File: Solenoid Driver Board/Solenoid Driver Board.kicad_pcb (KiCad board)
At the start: 2 copper layers, 33.5 x 39.6 mm, 22 parts, among them J2 Solenoid, Q1 IRLB8721PBF, U1 AMS1117-5.0, U2 STM8S003F3P, Y1 Crystal

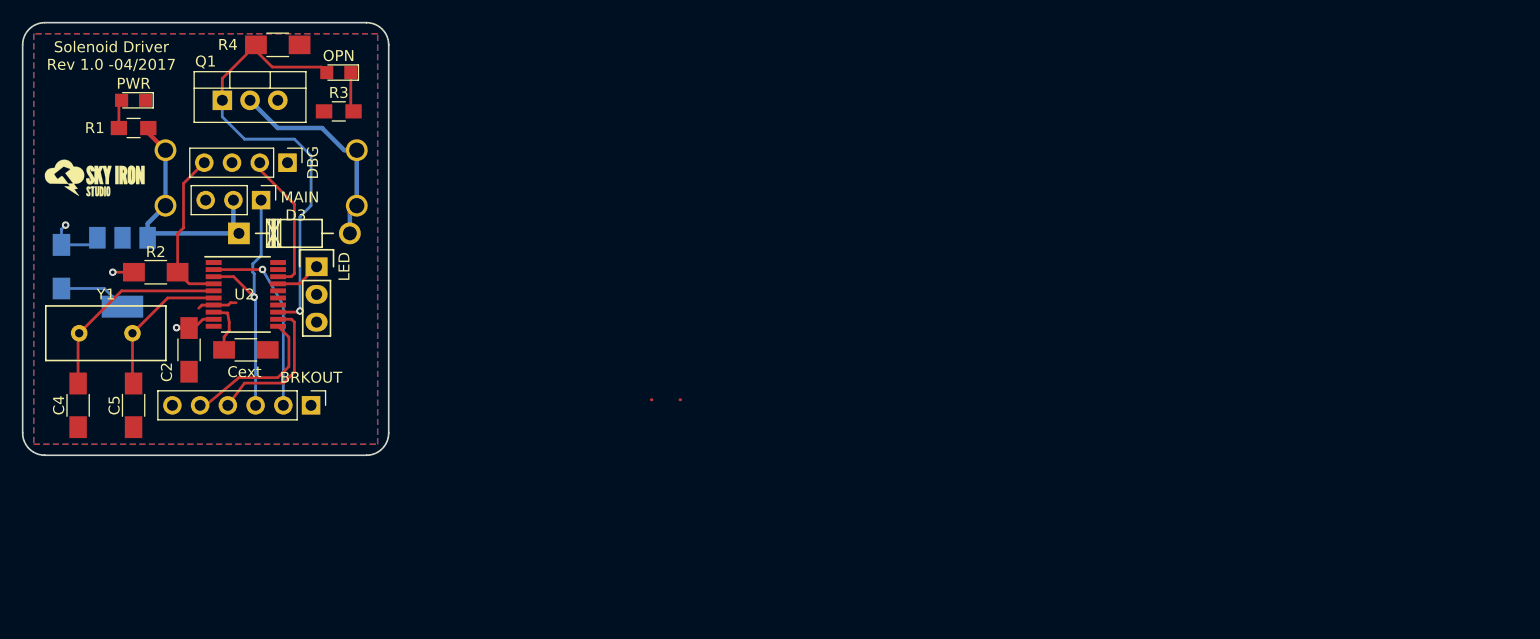
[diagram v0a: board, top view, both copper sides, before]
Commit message: Moved fade to TIM4, started work on new board revision
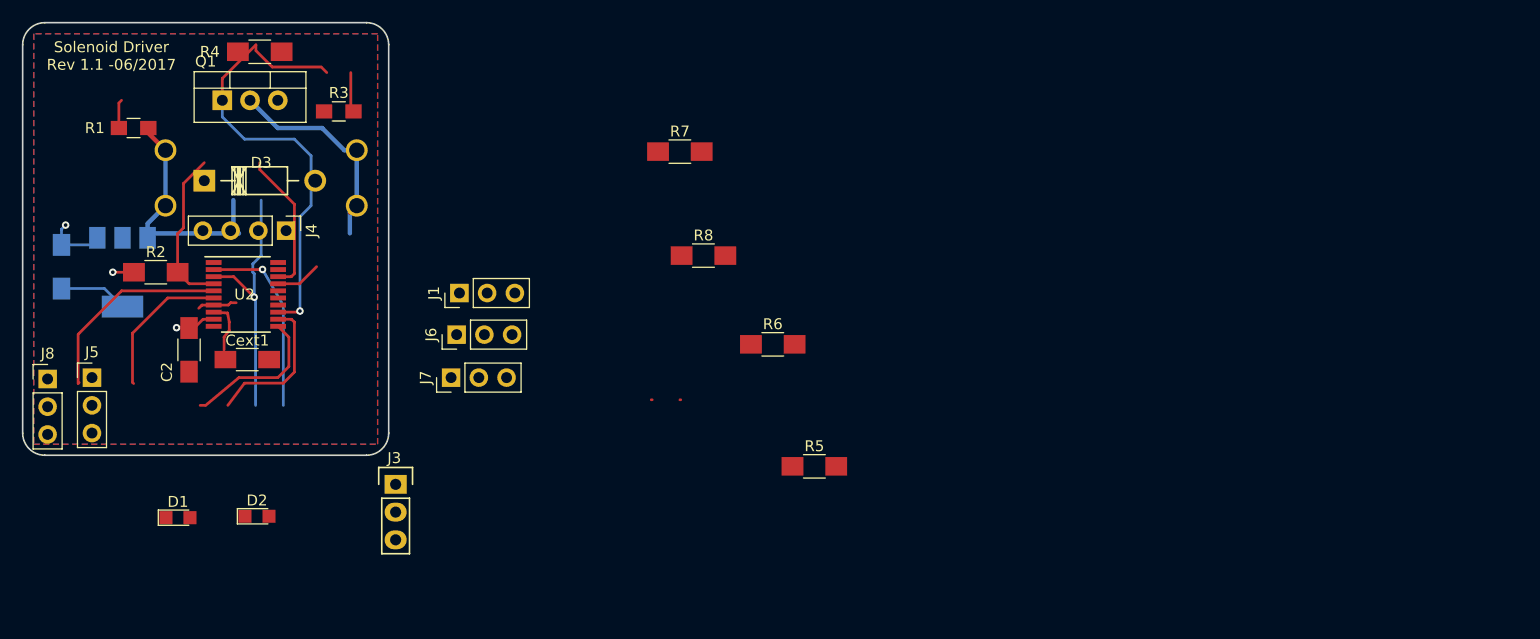
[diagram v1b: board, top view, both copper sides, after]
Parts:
- removed BRKOUT: BREAKOUT, Pin_Headers:Pin_Header_Straight_1x06_Pitch2.54mm
- removed C4, C5: 22pf, Capacitors_SMD:C_1206_HandSoldering
- removed Cext: 1 uF, Capacitors_SMD:C_1206_HandSoldering
- removed DBG: DEBUG, Pin_Headers:Pin_Header_Straight_1x04_Pitch2.54mm
- removed G***: LOGO, Modules:SkyIronLogo
- removed LED: RGB_LED, Pin_Headers:Pin_Header_Straight_1x03
- removed MAIN: MAIN, Pin_Headers:Pin_Header_Straight_1x03_Pitch2.54mm
- removed OPN: ON, LEDs:LED_0805
- removed PWR: PWR, LEDs:LED_0805
- removed Y1: Crystal, SpadeConnector:Crystal_HC-49-S
- added Cext1: 1 uF, Capacitors_SMD:C_1206_HandSoldering, F.Cu at (119.1, 103.0)
- added D1: PWR, LEDs:LED_0805, F.Cu at (112.8, 117.5)
- added D2: ON, LEDs:LED_0805, F.Cu at (120.0, 117.3)
- added J1: CH1, Pin_Headers:Pin_Header_Straight_1x03_Pitch2.54mm, F.Cu at (138.6, 96.9)
- added J3: RGB_LED, Pin_Headers:Pin_Header_Straight_1x03, F.Cu at (132.7, 114.4)
- added J4: DEBUG, Pin_Headers:Pin_Header_Straight_1x04_Pitch2.54mm, F.Cu at (122.7, 91.2)
- added J5: MAIN, Pin_Headers:Pin_Header_Straight_1x03_Pitch2.54mm, F.Cu at (104.9, 104.6)
- added J6: CH2, Pin_Headers:Pin_Header_Straight_1x03_Pitch2.54mm, F.Cu at (138.3, 100.7)
- added J7: CH3, Pin_Headers:Pin_Header_Straight_1x03_Pitch2.54mm, F.Cu at (137.8, 104.6)
- added J8: MAIN, Pin_Headers:Pin_Header_Straight_1x03_Pitch2.54mm, F.Cu at (100.8, 104.8)
- added R5: 10k, Resistors_SMD:R_1206_HandSoldering, F.Cu at (171.1, 112.8)
- added R6: 10k, Resistors_SMD:R_1206_HandSoldering, F.Cu at (167.3, 101.6)
- added R7: 10k, Resistors_SMD:R_1206_HandSoldering, F.Cu at (158.8, 83.9)
- added R8: 10k, Resistors_SMD:R_1206_HandSoldering, F.Cu at (160.9, 93.5)
- moved D3 5.78 mm to (115.2, 86.6)
- moved R4 1.77 mm to (120.3, 74.8)
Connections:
- U2 pad 10: (no net) -> CH3
- U2 pad 11: PB5 -> (no net)
- U2 pad 12: PB4 -> (no net)
- U2 pad 15: (no net) -> CH1
- U2 pad 19: (no net) -> VIN_A
- U2 pad 2: TX -> (no net)
- U2 pad 20: (no net) -> CH2
- U2 pad 5: Net-(C4-Pad2) -> (no net)
- U2 pad 6: Net-(C5-Pad2) -> (no net)
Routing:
- net (no net): track 0.16 -> 77.0 mm, vias 0 -> 1
- net Net-(C4-Pad2): track 18.7 -> 0.00 mm
- net TX: track 17.4 -> 0.00 mm, vias 1 -> 0
- net PB4: track 13.7 -> 0.00 mm
- net PB5: track 13.6 -> 0.00 mm
- net Net-(C5-Pad2): track 13.4 -> 0.00 mm
- net GND: track 9.16 -> 12.4 mm
- net +12V: track 23.6 -> 20.4 mm
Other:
- board text added: "Solenoid Driver Rev 1.1 -06/2017"
- board text removed: "0V"
- board text removed: "12V"
- board text removed: "5V"
- board text removed: "DAT"
- board text removed: "GND"
- board text removed: "PB4"
- board text removed: "PB5"
- board text removed: "RX"
- board text removed: "SCL"
- board text removed: "SDA"
- board text removed: "SW"
- board text removed: "Solenoid Driver Rev 1.0 -04/2017"
- board text removed: "TX"
- board text removed: "~RST"

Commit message: Layout work begun on v1.1 of PCB
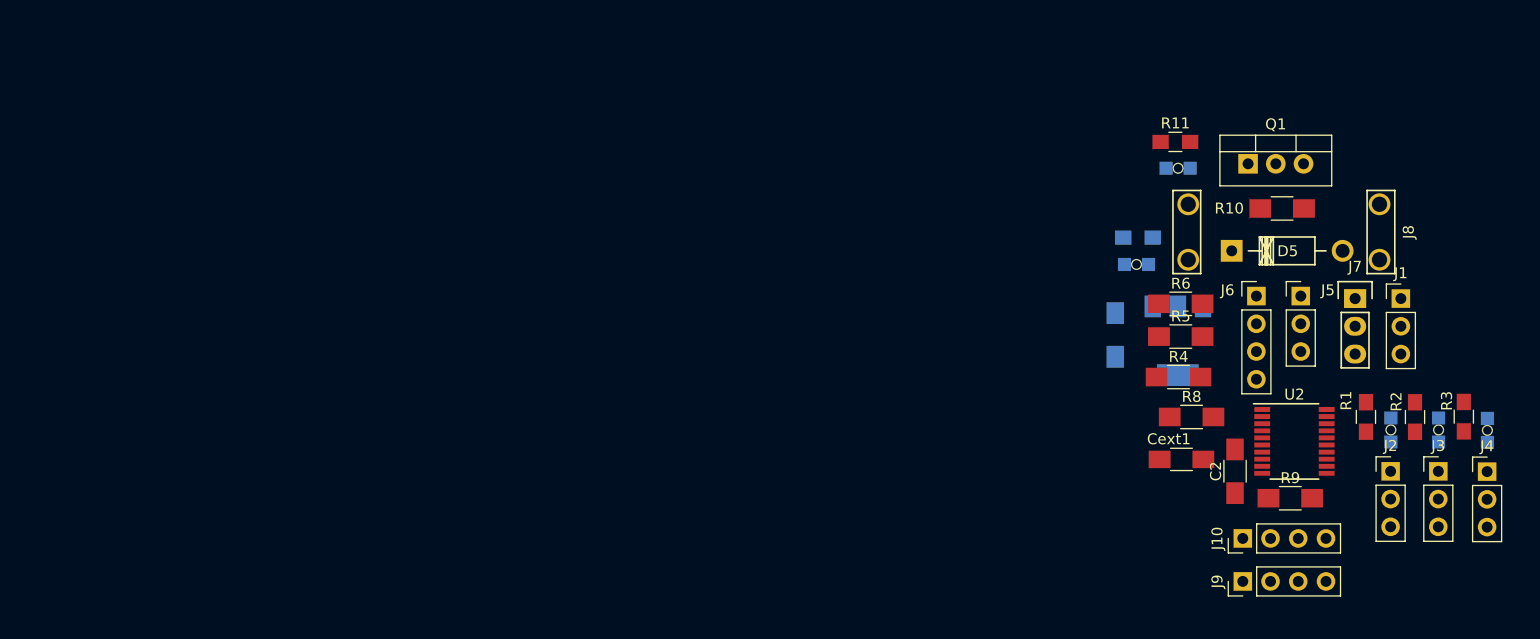
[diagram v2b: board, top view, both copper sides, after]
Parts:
- added D4: PWR, SpadeConnector:LED_0805_Bottom_Hole, B.Cu at (200.6, 94.3)
- added D5: 1N4007, Diodes_THT:Diode_DO-41_SOD81_Horizontal_RM10, F.Cu at (209.3, 93.0)
- added D6: ON, SpadeConnector:LED_0805_Bottom_Hole, B.Cu at (204.4, 85.5)
- added J10: DEBUG, Pin_Headers:Pin_Header_Straight_1x04_Pitch2.54mm, F.Cu at (210.3, 119.4)
- added J9: I2C, Pin_Headers:Pin_Header_Straight_1x04_Pitch2.54mm, F.Cu at (210.3, 123.3)
- added R10: 10K, Resistors_SMD:R_1206_HandSoldering, F.Cu at (213.9, 89.2)
- added R11: 330, Resistors_SMD:R_0805_HandSoldering, F.Cu at (204.1, 83.1)
- added R9: 10k, Resistors_SMD:R_1206_HandSoldering, F.Cu at (214.7, 115.7)
- D1: value PWR -> ON; footprint LEDs:LED_0805 -> SpadeConnector:LED_0805_Bottom_Hole; moved to B.Cu
- D2: footprint LEDs:LED_0805 -> SpadeConnector:LED_0805_Bottom_Hole; moved to B.Cu
- D3: value 1N4007 -> ON; footprint Diodes_THT:Diode_DO-41_SOD81_Horizontal_RM10 -> SpadeConnector:LED_0805_Bottom_Hole; moved to B.Cu
- J1: value CH1 -> AIN2
- J2: value Solenoid -> CH1; footprint SpadeConnector:Spade_Conn_Solenoid -> Pin_Headers:Pin_Header_Straight_1x03_Pitch2.54mm; moved to F.Cu
- J3: value RGB_LED -> CH2; footprint Pin_Headers:Pin_Header_Straight_1x03 -> Pin_Headers:Pin_Header_Straight_1x03_Pitch2.54mm
- J4: value DEBUG -> CH3; footprint Pin_Headers:Pin_Header_Straight_1x04_Pitch2.54mm -> Pin_Headers:Pin_Header_Straight_1x03_Pitch2.54mm
- J5: value MAIN -> BUS-O
- J6: value CH2 -> BUS-I; footprint Pin_Headers:Pin_Header_Straight_1x03_Pitch2.54mm -> Pin_Headers:Pin_Header_Straight_1x04_Pitch2.54mm
- J7: value CH3 -> RGB_LED; footprint Pin_Headers:Pin_Header_Straight_1x03_Pitch2.54mm -> Pin_Headers:Pin_Header_Straight_1x03
- J8: value MAIN -> Solenoid; footprint Pin_Headers:Pin_Header_Straight_1x03_Pitch2.54mm -> SpadeConnector:Spade_Conn_Solenoid
- R1: value 900 -> 330
- R2: value 10k -> 330; footprint Resistors_SMD:R_1206_HandSoldering -> Resistors_SMD:R_0805_HandSoldering
- R3: value 290 -> 330
- R4: value 10K -> 10k
- R7: value 10k -> 1k; footprint Resistors_SMD:R_1206_HandSoldering -> Resistors_SMD:R_0805_HandSoldering; moved to B.Cu
- moved D3 119.7 mm to (232.7, 109.5), turned to 270 degrees
- moved R2 116.1 mm to (226.1, 108.3), turned to 270 degrees
- moved R1 115.9 mm to (221.6, 108.3), turned to 270 degrees
- moved J8 114.0 mm to (214.1, 91.3)
- moved J4 112.2 mm to (232.7, 113.3), turned to 0 degrees
- moved D1 111.4 mm to (223.9, 109.4), turned to 270 degrees
- moved J5 111.0 mm to (215.6, 97.2)
- moved D2 108.5 mm to (228.2, 109.4), turned to 270 degrees
- moved J2 106.9 mm to (223.9, 113.2)
- moved R3 106.8 mm to (230.6, 108.2), turned to 270 degrees
- moved U2 97.0 mm to (215.0, 110.5)
- moved U1 96.9 mm to (204.4, 101.3)
- moved C1 96.7 mm to (198.6, 100.7)
- moved C2 96.5 mm to (209.6, 113.2), turned to 90 degrees
- moved J3 95.5 mm to (228.2, 113.2)
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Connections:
- D1 pad 1: GND -> Net-(D1-Pad1)
- D1 pad 2: Net-(D1-Pad2) -> CH1
- D2 pad 2: PC3 -> CH2
- D3 pad 1: +12V -> Net-(D3-Pad1)
- D3 pad 2: Net-(D3-Pad2) -> CH3
- J1 pad 1: CH1 -> AIN2
- J2 pad 1: +12V -> CH1
- J2 pad 2: Net-(D3-Pad2) -> +5V
- J3 pad 1: Net-(J3-Pad1) -> CH2
- J4 pad 1: +5V -> CH3
- J4 pad 2: SWIM -> +5V
- J6 pad 1: CH2 -> RX
- J6 pad 2: +5V -> +12V
- J7 pad 1: CH3 -> Net-(J7-Pad1)
- J8 pad 1: RX -> +12V
- J8 pad 2: +12V -> Net-(D5-Pad2)
- Q1 pad 2: Net-(D3-Pad2) -> Net-(D5-Pad2)
- R1 pad 1: +12V -> GND
- R1 pad 2: Net-(D1-Pad2) -> Net-(D1-Pad1)
- R2 pad 1: +5V -> GND
- R2 pad 2: NRST -> Net-(D2-Pad1)
- R3 pad 2: Net-(D2-Pad1) -> Net-(D3-Pad1)
- R4 pad 1: GND -> Net-(R4-Pad1)
- R4 pad 2: PC3 -> VIN_A
- R5 pad 1: VIN_A -> Net-(R4-Pad1)
- R6 pad 1: Net-(R5-Pad2) -> +12V
- R6 pad 2: Net-(R6-Pad2) -> Net-(R5-Pad2)
- R7 pad 2: Net-(R6-Pad2) -> Net-(D4-Pad2)
- U2 pad 10: CH3 -> CH1
- U2 pad 11: (no net) -> SDA
- U2 pad 12: (no net) -> SCL
- U2 pad 14: (no net) -> AIN2
- U2 pad 15: CH1 -> CH2
- U2 pad 17: Net-(J3-Pad1) -> Net-(J7-Pad1)
- U2 pad 2: (no net) -> TX
- U2 pad 20: CH2 -> CH3
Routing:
- net (no net): track 77.0 -> 0.00 mm, vias 1 -> 0
- net PC3: track 42.0 -> 0.00 mm, vias 1 -> 0
- net RX: track 23.7 -> 0.00 mm, vias 1 -> 0
- net Net-(D3-Pad2): track 21.8 -> 0.00 mm
- net +12V: track 20.4 -> 0.00 mm
- net NRST: track 14.8 -> 0.00 mm
- net SWIM: track 13.1 -> 0.00 mm
- net +5V: track 12.9 -> 0.00 mm, vias 2 -> 0
- net GND: track 12.4 -> 0.00 mm, vias 1 -> 0
- net Net-(Cext1-Pad1): track 4.83 -> 0.00 mm
- net Net-(J3-Pad1): track 4.18 -> 0.00 mm
- net Net-(D2-Pad1): track 3.66 -> 0.00 mm
- net Net-(D1-Pad2): track 2.64 -> 0.00 mm
- removed copper zone on B.Cu, net +5V
- removed copper zone on F.Cu, net GND
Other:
- board outline removed
- board text removed: "Solenoid Driver Rev 1.1 -06/2017"

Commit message: New source image
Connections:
- D1 pad 2: CH1 -> CH0
- D2 pad 2: CH2 -> CH1
- D3 pad 2: CH3 -> CH2
- J2 pad 1: CH1 -> CH0
- J3 pad 1: CH2 -> CH1
- J4 pad 1: CH3 -> CH2
- U2 pad 10: CH1 -> CH0
- U2 pad 15: CH2 -> CH1
- U2 pad 20: CH3 -> CH2

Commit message: PWM Test, lots of work on v1.1 PCBs
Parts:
- added REF**: MountingHole_3.2mm_M3, Mounting_Holes:MountingHole_3.2mm_M3, F.Cu at (229.4, 85.5)
- added REF**: MountingHole_3.2mm_M3, Mounting_Holes:MountingHole_3.2mm_M3, F.Cu at (202.4, 120.5)
- moved P2 3.65 mm to (229.1, 113.8)
- moved P1 1.77 mm to (226.5, 113.8)
- moved R8 1.37 mm to (204.6, 107.3)
- moved C2 0.99 mm to (209.6, 112.2)
- moved P0 0.58 mm to (224.0, 113.8)
- renumbered J1 to AIN2, J10 to DBG, J9 to I2C, J6 to IN, J7 to LED, J5 to OUT, J2 to P0, J3 to P1, J4 to P2
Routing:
- net PC3: track 0.00 -> 41.0 mm, vias 0 -> 2
- net +12V: track 0.00 -> 37.5 mm
- net CH2: track 0.00 -> 20.8 mm
- net Net-(D5-Pad2): track 0.00 -> 19.3 mm
- net AIN2: track 0.00 -> 18.9 mm, vias 0 -> 1
- net RX: track 0.00 -> 18.1 mm
- net SCL: track 0.00 -> 17.7 mm
- net NRST: track 0.00 -> 17.3 mm
- net CH0: track 0.00 -> 16.2 mm, vias 0 -> 1
- net SWIM: track 0.00 -> 15.5 mm
- net CH1: track 0.00 -> 14.9 mm
- net VIN_A: track 0.00 -> 14.5 mm, vias 0 -> 2
- net Net-(J7-Pad1): track 0.00 -> 14.5 mm, vias 0 -> 2
- net GND: track 0.00 -> 13.7 mm, vias 0 -> 1
- net SDA: track 0.00 -> 11.4 mm
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- added copper zone on B.Cu, net +5V
- added copper zone on F.Cu, net GND
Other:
- board outline added: 39.4 x 47 mm
- board text added: "Solenoid Driver Rev 1.1 07/2017"
